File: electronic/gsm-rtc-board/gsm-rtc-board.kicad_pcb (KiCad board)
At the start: 2 copper layers, 43 x 85 mm, 13 parts, among them J1 Power, J2 GSM, J3 Raspberry, J4 RTC

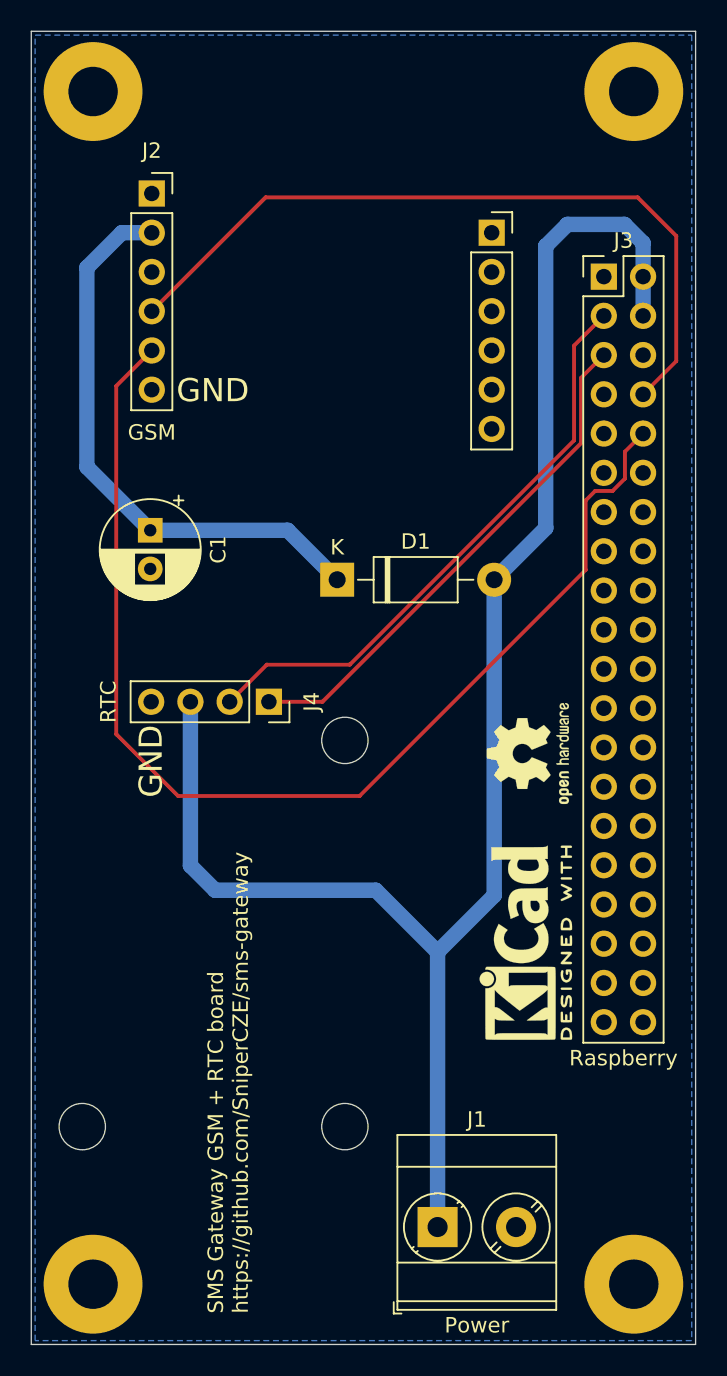
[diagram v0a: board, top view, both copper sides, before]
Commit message: rtc mounting holes
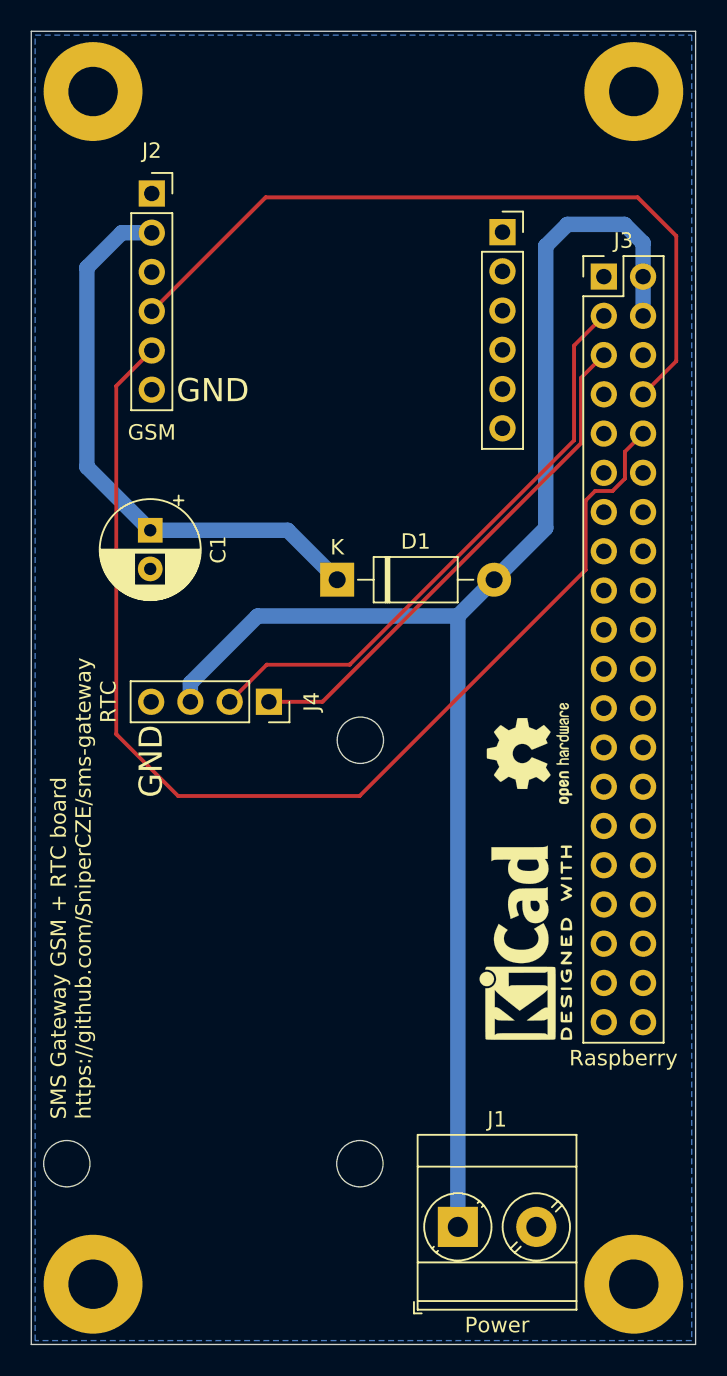
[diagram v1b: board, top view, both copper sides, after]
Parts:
- moved J1 1.31 mm to (97.6, 142.4)
- moved REF** 0.70 mm to (100.5, 78.0)
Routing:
- net +5V: track 107.4 -> 98.3 mm
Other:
- outline, holes or cut-outs redrawn

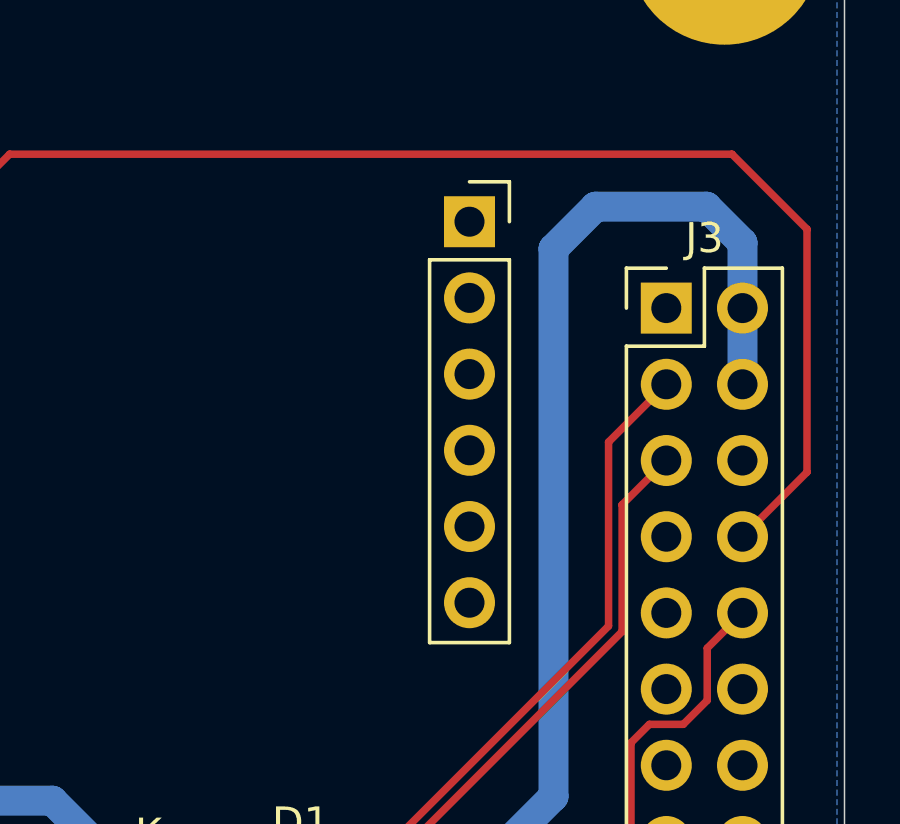
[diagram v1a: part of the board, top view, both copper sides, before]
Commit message: GSM sockets slightly off
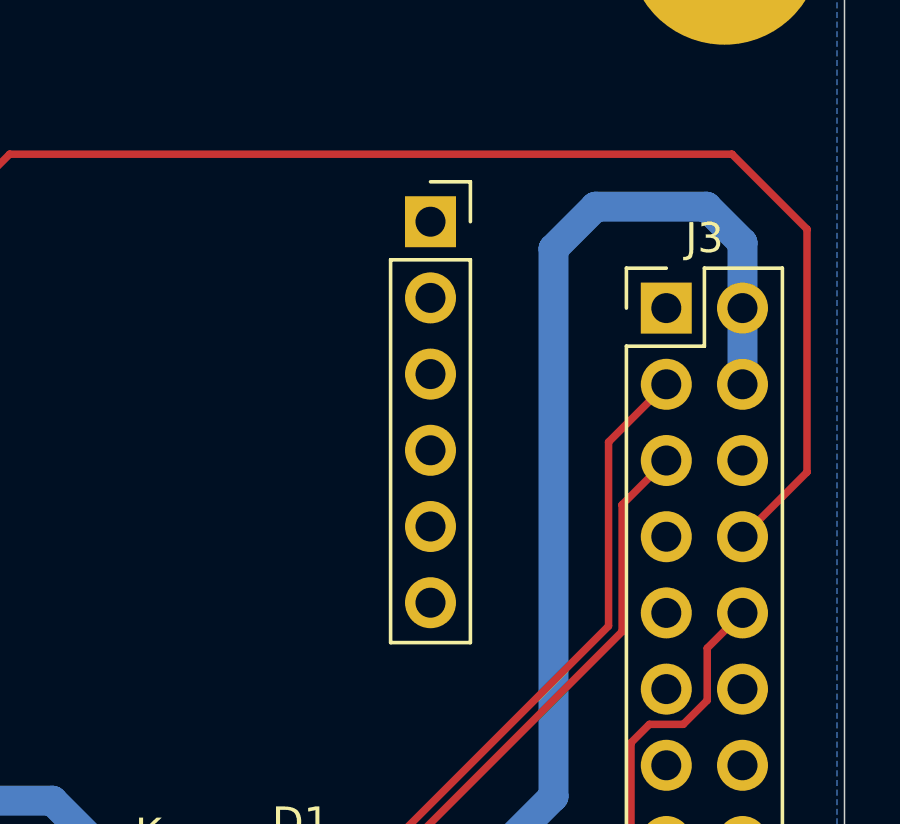
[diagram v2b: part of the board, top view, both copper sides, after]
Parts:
- moved REF** 1.30 mm to (99.2, 78.0)
